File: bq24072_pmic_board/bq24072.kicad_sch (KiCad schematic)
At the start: 11 parts, among them U201 BQ24072RGT

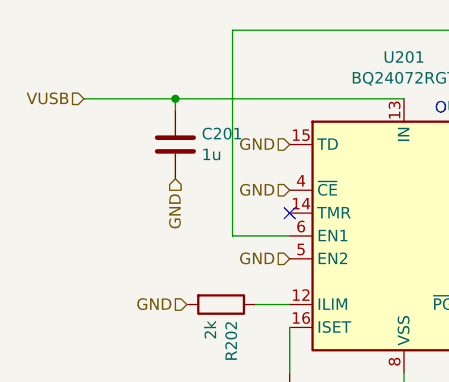
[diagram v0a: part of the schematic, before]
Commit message: [bq24072_pmic_board] Add VBUS output and bump board revision to v2
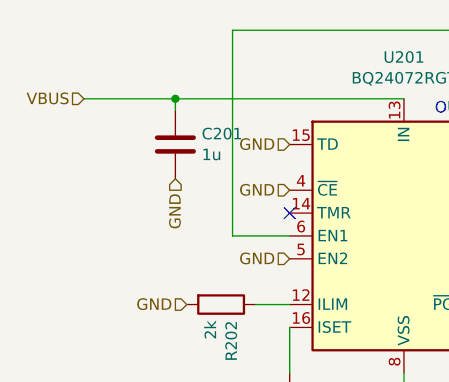
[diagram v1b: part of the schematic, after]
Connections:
- net VUSB renamed VBUS
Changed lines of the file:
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@@
     (effects (font (size 1.27 1.27)) (justify right))
   )
-  (hierarchical_label "VUSB" (shape input) (at 81.28 78.74 180)
+  (hierarchical_label "VBUS" (shape input) (at 81.28 78.74 180)
     (effects (font (size 1.27 1.27)) (justify right))
   )
